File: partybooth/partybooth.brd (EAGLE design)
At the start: 61.6 x 39 mm, 26 parts, among them IC1 TINY13-20PU, IC2 78L05Z, J1 Lamp, J2 Button, J3 12V, T1 2N3904, T2 2N3904, X1 1501_06

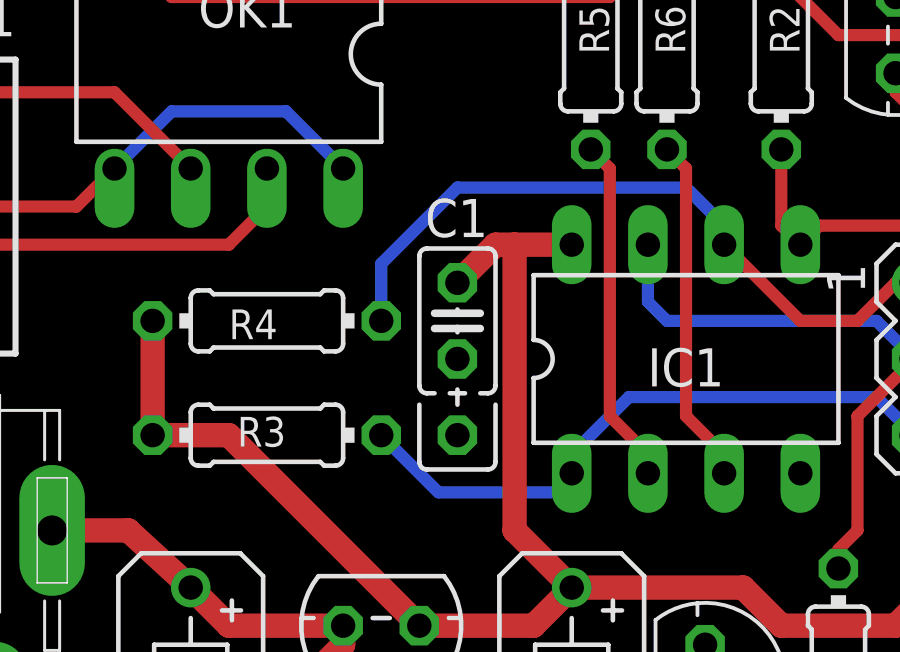
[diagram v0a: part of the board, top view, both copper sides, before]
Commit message: 
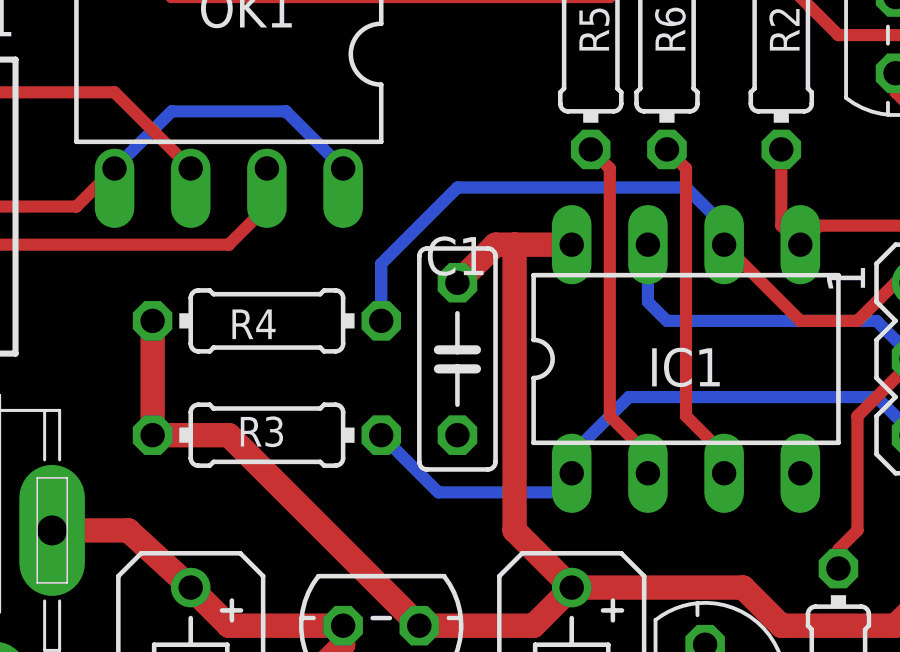
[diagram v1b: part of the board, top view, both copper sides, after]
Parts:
- C1: device rcl:C025_050-025X075 -> rcl:C050-025X075
- moved C1 1.27 mm to (24.1, 20.3)
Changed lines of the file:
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@@
 <attribute name="VALUE" x="44.069" y="20.955" size="1.27" layer="27" ratio="10" rot="R270"/>
 </element>
-<element name="C1" library="rcl" package="C025_050-025X075" value="0.1u" x="24.13" y="21.59" smashed="yes" rot="R270">
-<attribute name="NAME" x="25.146" y="25.654" size="1.27" layer="25" ratio="10" rot="R180"/>
+<element name="C1" library="rcl" package="C050-025X075" value="0.1u" x="24.13" y="20.32" smashed="yes" rot="R270">
+<attribute name="NAME" x="25.146" y="24.384" size="1.27" layer="25" ratio="10" rot="R180"/>
 </element>
 <element name="X1" library="con-lumberg" package="1501_06" value="1501_06" x="0" y="25.4" smashed="yes" rot="R90">

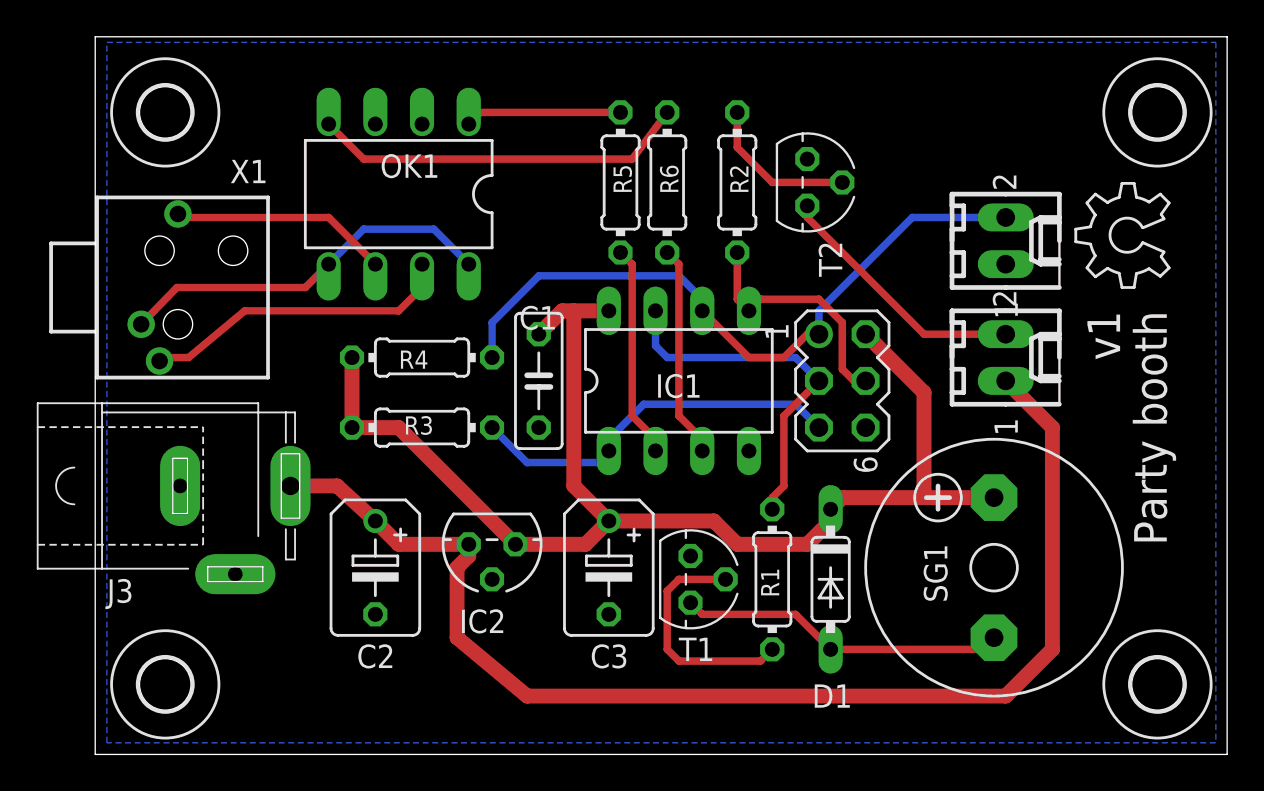
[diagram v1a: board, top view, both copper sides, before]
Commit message: 
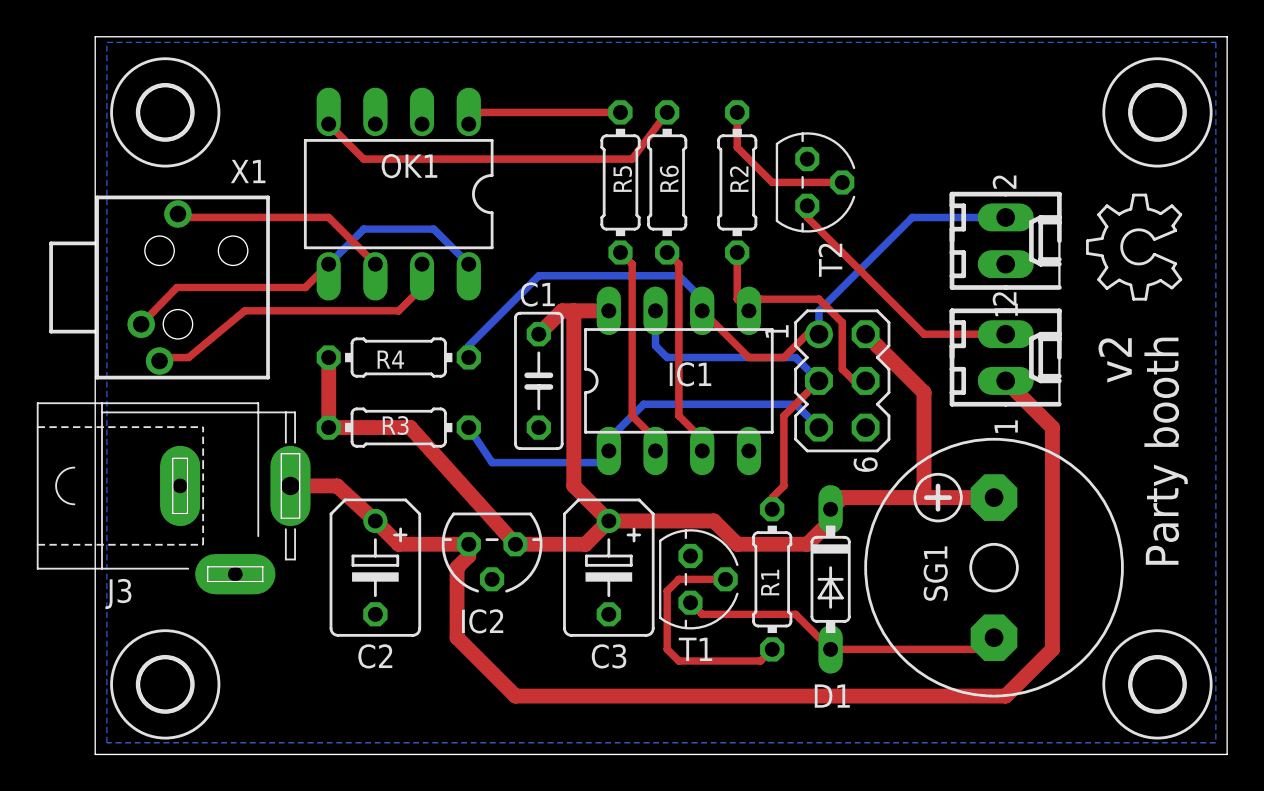
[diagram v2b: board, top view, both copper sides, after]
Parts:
- moved R3 1.27 mm to (16.5, 17.8)
- moved R4 1.27 mm to (16.5, 21.6)
- moved U$1 0.90 mm to (59.1, 24.8)
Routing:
- net N$6: track 21.2 -> 22.7 mm
- net +5V: track 70.6 -> 72.1 mm
- net BTN: track 37.0 -> 37.5 mm
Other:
- board text added: "v2"
- board text removed: "v1"
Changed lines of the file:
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@@
 <wire x1="61.575" y1="39.04" x2="0" y2="39.04" width="0" layer="20"/>
 <wire x1="0" y1="39.04" x2="0" y2="0" width="0" layer="20"/>
-<text x="56.515" y="24.13" size="1.778" layer="21" rot="R270">Party booth</text>
-<text x="53.975" y="24.13" size="1.778" layer="21" rot="R270">v1</text>
+<text x="57.15" y="22.86" size="1.778" layer="21" rot="R270">Party booth</text>
+<text x="54.61" y="22.86" size="1.778" layer="21" rot="R270">v2</text>
 </plain>
 <attributes>
@@
 <attribute name="MF" value="" x="69.85" y="-2.54" size="1.778" layer="27" display="off"/>
 <attribute name="OC_FARNELL" value="9171550" x="69.85" y="-2.54" size="1.778" layer="27" display="off"/>
-<attribute name="NAME" x="33.02" y="20.6756" size="1.27" layer="25" ratio="10" rot="R180"/>
+<attribute name="NAME" x="33.655" y="21.3106" size="1.27" layer="25" ratio="10" rot="R180"/>
 </element>
 <element name="OK1" library="optocoupler" package="DIL08" value="" x="16.51" y="30.48" smashed="yes" rot="R180">
@@
 </element>
 <element name="C1" library="rcl" package="C050-025X075" value="0.1u" x="24.13" y="20.32" smashed="yes" rot="R270">
-<attribute name="NAME" x="25.146" y="24.384" size="1.27" layer="25" ratio="10" rot="R180"/>
+<attribute name="NAME" x="25.146" y="25.654" size="1.27" layer="25" ratio="10" rot="R180"/>
 </element>
 <element name="X1" library="con-lumberg" package="1501_06" value="1501_06" x="0" y="25.4" smashed="yes" rot="R90">
@@
 <attribute name="NAME" x="26.924" y="4.699" size="1.27" layer="25" ratio="10"/>
 </element>
-<element name="R3" library="rcl" package="0204/7" value="10k" x="17.78" y="17.78" smashed="yes" rot="R180">
-<attribute name="NAME" x="18.415" y="18.3896" size="0.9906" layer="25" ratio="10" rot="R180"/>
-</element>
-<element name="R4" library="rcl" package="0204/7" value="10k" x="17.78" y="21.59" smashed="yes" rot="R180">
-<attribute name="NAME" x="16.51" y="20.9804" size="0.9906" layer="25" ratio="10"/>
+<element name="R3" library="rcl" package="0204/7" value="10k" x="16.51" y="17.78" smashed="yes" rot="R180">
+<attribute name="NAME" x="17.145" y="18.3896" size="0.9906" layer="25" ratio="10" rot="R180"/>
+</element>
+<element name="R4" library="rcl" package="0204/7" value="10k" x="16.51" y="21.59" smashed="yes" rot="R180">
+<attribute name="NAME" x="15.24" y="20.9804" size="0.9906" layer="25" ratio="10"/>
 </element>
 <element name="R5" library="rcl" package="0204/7" value="220" x="28.575" y="31.115" smashed="yes" rot="R90">
@@
 <attribute name="NAME" x="0.635" y="8.255" size="1.27" layer="25"/>
 </element>
-<element name="U$1" library="ohw-logo" package="OSHW_6X200_NOTEXT" value="" x="58.42" y="25.4" rot="R90"/>
+<element name="U$1" library="ohw-logo" package="OSHW_6X200_NOTEXT" value="" x="59.055" y="24.765" rot="R90"/>
 <element name="U$2" library="holes" package="2,8" value="" x="3.81" y="34.925"/>
 <element name="U$3" library="holes" package="2,8" value="" x="57.785" y="34.925"/>
@@
 <contactref element="IC2" pad="1"/>
 <contactref element="R4" pad="2"/>
-<wire x1="22.86" y1="11.43" x2="16.51" y2="17.78" width="0.8128" layer="1"/>
-<wire x1="16.51" y1="17.78" x2="13.97" y2="17.78" width="0.8128" layer="1"/>
-<wire x1="13.97" y1="17.78" x2="13.97" y2="21.59" width="0.8128" layer="1"/>
+<wire x1="22.86" y1="11.43" x2="17.145" y2="17.78" width="0.8128" layer="1"/>
+<wire x1="17.145" y1="17.78" x2="12.7" y2="17.78" width="0.8128" layer="1"/>
+<wire x1="12.7" y1="17.78" x2="12.7" y2="21.59" width="0.8128" layer="1"/>
 <wire x1="22.86" y1="11.43" x2="26.67" y2="11.43" width="0.8128" layer="1"/>
 <wire x1="26.67" y1="11.43" x2="27.94" y2="12.7" width="0.8128" layer="1"/>
@@
 <wire x1="52.07" y1="17.78" x2="52.07" y2="5.715" width="0.8128" layer="1"/>
 <wire x1="52.07" y1="5.715" x2="49.53" y2="3.175" width="0.8128" layer="1"/>
-<wire x1="49.53" y1="3.175" x2="23.495" y2="3.175" width="0.8128" layer="1"/>
-<wire x1="23.495" y1="3.175" x2="19.685" y2="6.35" width="0.8128" layer="1"/>
+<wire x1="49.53" y1="3.175" x2="22.86" y2="3.175" width="0.8128" layer="1"/>
+<wire x1="22.86" y1="3.175" x2="19.685" y2="6.35" width="0.8128" layer="1"/>
 <wire x1="19.685" y1="6.35" x2="19.685" y2="10.16" width="0.8128" layer="1"/>
 <wire x1="19.685" y1="10.16" x2="20.32" y2="10.795" width="0.8128" layer="1"/>
@@
 <wire x1="29.845" y1="19.05" x2="27.94" y2="17.145" width="0.4064" layer="16"/>
 <wire x1="27.94" y1="17.145" x2="27.94" y2="16.51" width="0.4064" layer="16"/>
-<wire x1="21.59" y1="17.78" x2="23.495" y2="15.875" width="0.4064" layer="16"/>
-<wire x1="23.495" y1="15.875" x2="27.94" y2="15.875" width="0.4064" layer="16"/>
+<wire x1="20.32" y1="17.78" x2="21.59" y2="15.875" width="0.4064" layer="16"/>
+<wire x1="21.59" y1="15.875" x2="27.94" y2="15.875" width="0.4064" layer="16"/>
 <wire x1="27.94" y1="15.875" x2="27.94" y2="16.51" width="0.4064" layer="16"/>
 </signal>
@@
 <wire x1="44.45" y1="29.21" x2="39.37" y2="24.13" width="0.4064" layer="16"/>
 <wire x1="39.37" y1="24.13" x2="39.37" y2="22.86" width="0.4064" layer="16"/>
-<wire x1="21.59" y1="23.495" x2="24.13" y2="26.035" width="0.4064" layer="16"/>
+<wire x1="20.32" y1="22.225" x2="24.13" y2="26.035" width="0.4064" layer="16"/>
 <wire x1="24.13" y1="26.035" x2="31.75" y2="26.035" width="0.4064" layer="16"/>
 <wire x1="31.75" y1="26.035" x2="33.02" y2="24.765" width="0.4064" layer="16"/>
@@
 <contactref element="J2" pad="2"/>
 <wire x1="49.53" y1="29.21" x2="44.45" y2="29.21" width="0.4064" layer="16"/>
-<wire x1="21.59" y1="23.495" x2="21.59" y2="21.59" width="0.4064" layer="16"/>
+<wire x1="20.32" y1="22.225" x2="20.32" y2="21.59" width="0.4064" layer="16"/>
 </signal>
 </signals>
